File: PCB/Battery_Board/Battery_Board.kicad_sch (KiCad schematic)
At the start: 8 parts, among them J1 SE2-30, U1 LTC4451AV-TRPBF

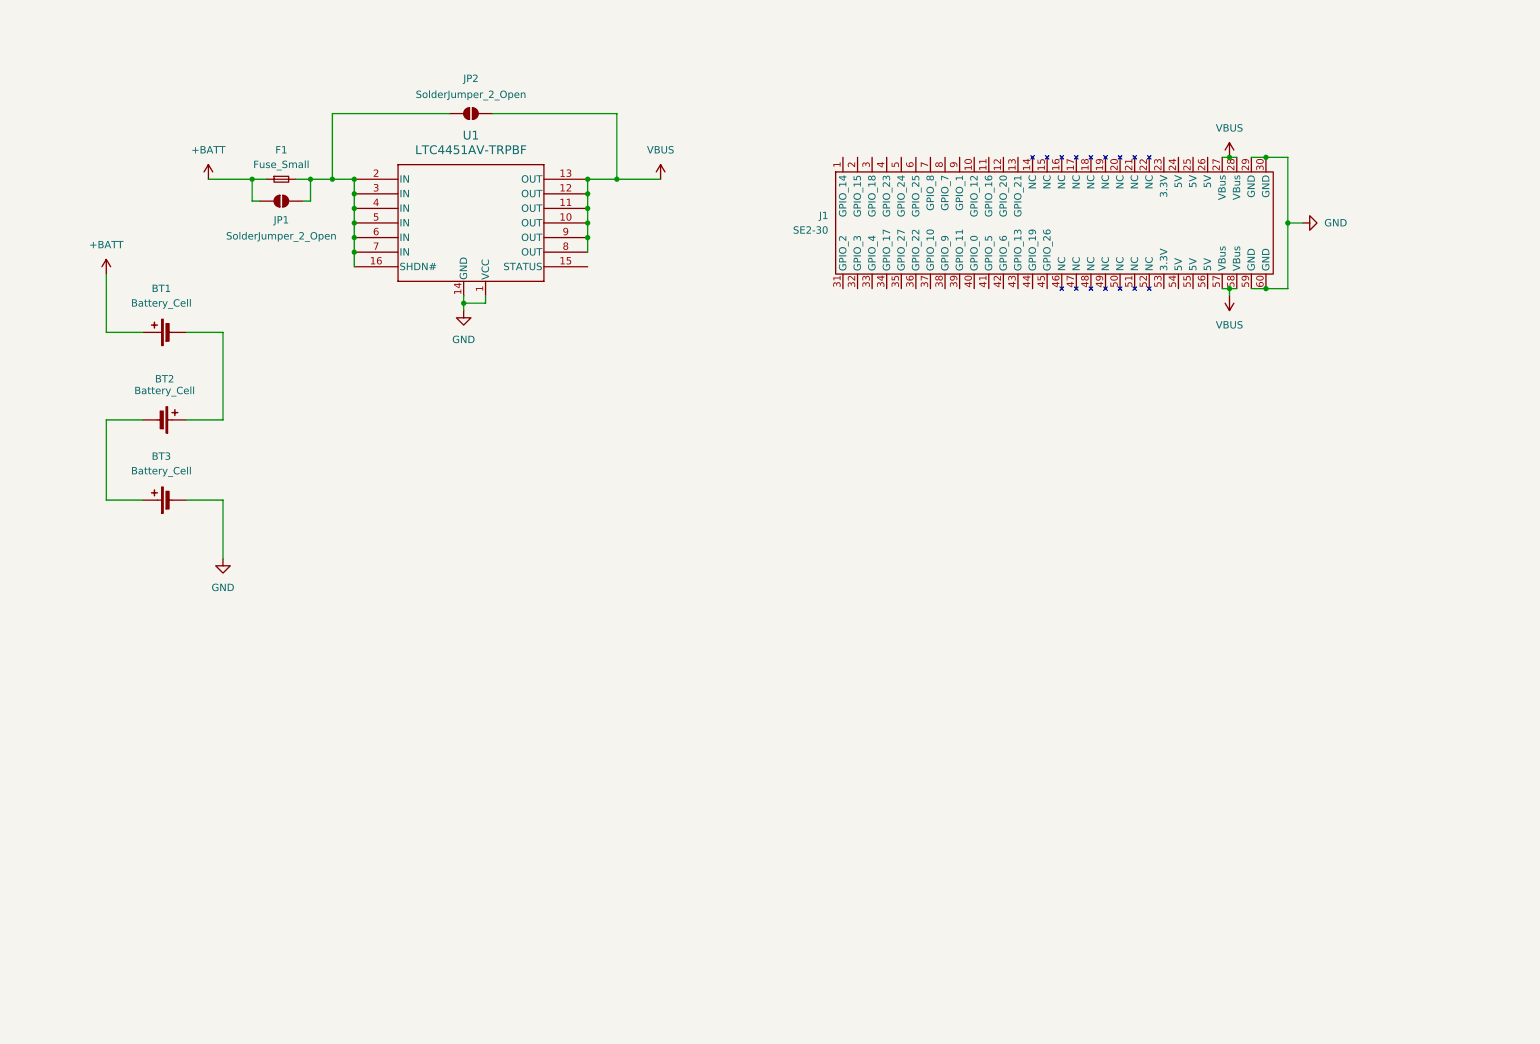
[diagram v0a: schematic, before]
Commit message: Updated battery board to include ATtiny MCU for current and voltage monitoring. Updated SE2-30 footprint's silkscreen.
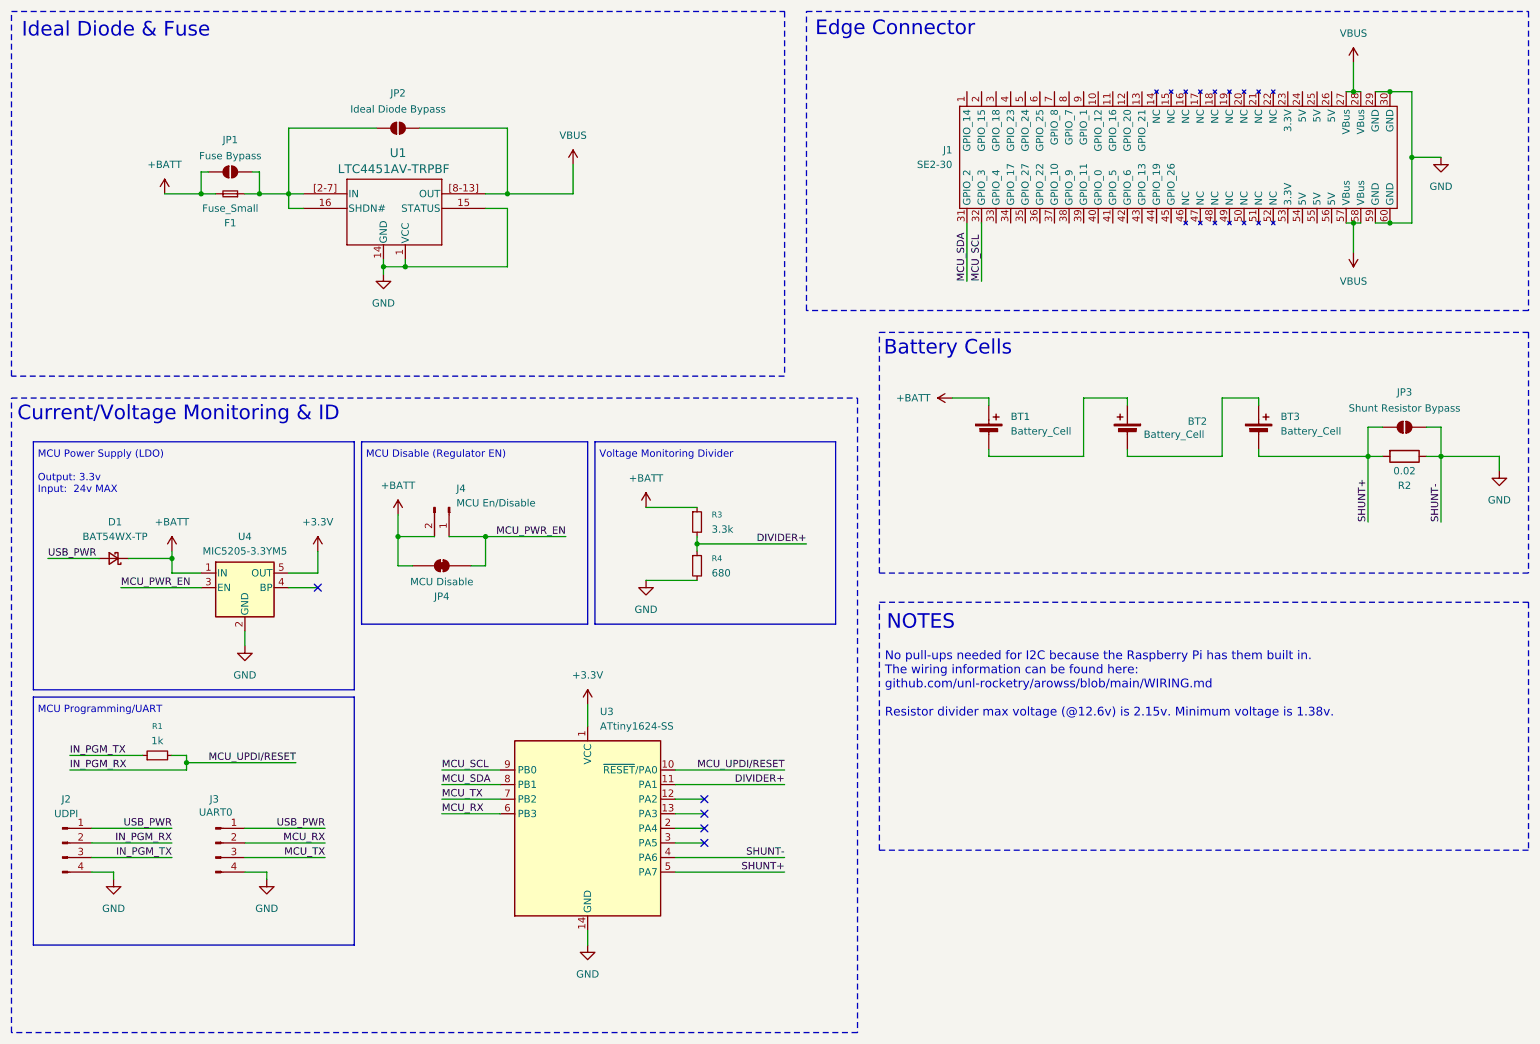
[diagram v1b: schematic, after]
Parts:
- added D1: BAT54WX-TP, Diode_SMD:D_SOD-523, symbol Device:D_Schottky_Small
- added J2: UDPI, Connector_PinHeader_2.54mm:PinHeader_1x04_P2.54mm_Vertical, symbol Connector:Conn_01x04_Pin
- added J3: UART0, Connector_PinHeader_2.54mm:PinHeader_1x04_P2.54mm_Vertical, symbol Connector:Conn_01x04_Pin
- added J4: MCU En/Disable, Connector_PinHeader_2.54mm:PinHeader_1x02_P2.54mm_Vertical, symbol Connector:Conn_01x02_Pin
- added JP3: Shunt Resistor Bypass, Jumper:SolderJumper-2_P1.3mm_Open_TrianglePad1.0x1.5mm, symbol Jumper:SolderJumper_2_Open
- added JP4: MCU Disable, Jumper:SolderJumper-2_P1.3mm_Bridged_RoundedPad1.0x1.5mm, symbol Jumper:SolderJumper_2_Bridged
- added R1: 1k, Resistor_SMD:R_0603_1608Metric, symbol Device:R_Small
- added R2: 0.02, Resistor_SMD:R_1206_3216Metric, symbol Device:R
- added R3: 3.3k, Resistor_SMD:R_0603_1608Metric, symbol Device:R_Small
- added R4: 680, Resistor_SMD:R_0603_1608Metric, symbol Device:R_Small
- added U3: ATtiny1624-SS, Package_SO:SOIC-14_3.9x8.7mm_P1.27mm, symbol MCU_Microchip_ATtiny:ATtiny1624-SS
- added U4: MIC5205-3.3YM5, Package_TO_SOT_SMD:SOT-23-5, symbol Regulator_Linear:MIC5205-3.3YM5
- JP1: value SolderJumper_2_Open -> Fuse Bypass
- JP2: value SolderJumper_2_Open -> Ideal Diode Bypass
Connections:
- net +BATT: now also F1.2, D1.1 (K), J4.2 (Pin_2), JP4.1 (A), R3.1, U4.1 (IN); no longer F1.1
- net GND: now also U1.15 (STATUS), J2.4 (Pin_4), J3.4 (Pin_4), JP3.2 (B), R2.1, R4.2, U3.14 (GND), U3.4 (PA6), U4.2 (GND); no longer BT3.2 (-)
- net VBUS: now also U1.[8-13] (OUT); no longer U1.10 (OUT), U1.11 (OUT), U1.12 (OUT), U1.13 (OUT), U1.8 (OUT), U1.9 (OUT)
- net MCU_SDA: now reaches J1.31 (GPIO_2)
- net MCU_SDA: now also U3.8 (PB1)
- net MCU_SCL: now reaches J1.32 (GPIO_3)
- net MCU_SCL: now also U3.9 (PB0)
- new net: F1.1, JP1.2 (B), JP2.1 (A), U1.16 (SHDN#), U1.[2-7] (IN)
- new net +3.3V: U3.1 (VCC), U4.5 (OUT)
- new net DIVIDER+: R3.2, R4.1, U3.11 (PA1)
- new net IN_PGM_RX: J2.2 (Pin_2), R1.2, U3.10 (~{RESET}/PA0)
- new net IN_PGM_TX: J2.3 (Pin_3), R1.1
- new net MCU_PWR_EN: J4.1 (Pin_1), JP4.2 (B), U4.3 (EN)
- new net MCU_RX: J3.2 (Pin_2), U3.6 (PB3)
- new net MCU_TX: J3.3 (Pin_3), U3.7 (PB2)
- new net SHUNT+: BT3.2 (-), JP3.1 (A), R2.2, U3.5 (PA7)
- new net USB_PWR: D1.2 (A), J2.1 (Pin_1), J3.1 (Pin_1)
- no-connect marks 0 -> 5
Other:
- note added: "Battery Cells"
- note added: "Current/Voltage Monitoring & ID"
- note added: "Edge Connector"
- note added: "Ideal Diode & Fuse"
- note added: "MCU Disable (Regulator EN)"
- note added: "MCU Power Supply (LDO) Output: 3.3v Input: 24v MAX"
- note added: "MCU Programming/UART"
- note added: "NOTES"
- note added: "Voltage Monitoring Divider"
- company: (none) -> UNL Aerospace Rocketry
- title: (none) -> Battery Board
- moved on the sheet: BT1, BT2, BT3, F1, J1, JP1, JP2
